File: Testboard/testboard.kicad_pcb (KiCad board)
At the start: 2 copper layers, 0 parts

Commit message: :sparkles: PCB layout for the testboard
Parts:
- added C1: 100n, Capacitor_THT:C_Disc_D4.3mm_W1.9mm_P5.00mm, F.Cu at (83.8, 111.7)
- added C2: 10n, Capacitor_THT:C_Disc_D4.3mm_W1.9mm_P5.00mm, F.Cu at (83.9, 102.9)
- added C3: 100n, Capacitor_THT:C_Disc_D4.3mm_W1.9mm_P5.00mm, F.Cu at (95.9, 106.7)
- added C4: 10n, Capacitor_THT:C_Disc_D4.3mm_W1.9mm_P5.00mm, F.Cu at (111.1, 99.0)
- added C5: 100n, Capacitor_THT:C_Disc_D4.3mm_W1.9mm_P5.00mm, F.Cu at (114.3, 101.7)
- added C6: 100n, Capacitor_THT:C_Disc_D4.3mm_W1.9mm_P5.00mm, F.Cu at (111.1, 101.6)
- added C7: 100n, Capacitor_THT:C_Disc_D4.3mm_W1.9mm_P5.00mm, F.Cu at (106.6, 95.2)
- added D1: rt, LED_THT:LED_D3.0mm, F.Cu at (107.3, 78.1)
- added J1: upper, Connector_PinSocket_2.54mm:PinSocket_2x02_P2.54mm_Vertical, F.Cu at (81.3, 79.5)
- added J2: lower, Connector_PinSocket_2.54mm:PinSocket_2x02_P2.54mm_Vertical, F.Cu at (81.3, 124.5)
- added J3: Out, Connector_PinHeader_2.54mm:PinHeader_1x02_P2.54mm_Vertical, F.Cu at (116.2, 78.7)
- added J4: Out, Connector_PinHeader_2.54mm:PinHeader_1x02_P2.54mm_Vertical, F.Cu at (112.4, 78.7)
- added J5: V_{drive}, Connector_PinHeader_2.54mm:PinHeader_1x02_P2.54mm_Vertical, F.Cu at (90.8, 118.7)
- added Q1: BC547, Package_TO_SOT_THT:TO-92_Inline, F.Cu at (98.4, 86.3)
- added R1: 100R, Resistor_THT:R_Axial_DIN0207_L6.3mm_D2.5mm_P7.62mm_Horizontal, F.Cu at (80.0, 114.2)
- added R10: 1k, Resistor_THT:R_Axial_DIN0207_L6.3mm_D2.5mm_P7.62mm_Horizontal, F.Cu at (103.5, 85.1)
- added R2: 2k2, Resistor_THT:R_Axial_DIN0207_L6.3mm_D2.5mm_P7.62mm_Horizontal, F.Cu at (80.0, 102.9)
- added R3: 10k, Resistor_THT:R_Axial_DIN0207_L6.3mm_D2.5mm_P7.62mm_Horizontal, F.Cu at (92.7, 102.9)
- added R4: 10k, Resistor_THT:R_Axial_DIN0207_L6.3mm_D2.5mm_P7.62mm_Horizontal, F.Cu at (92.7, 106.7)
- added R5: 4k7, Resistor_THT:R_Axial_DIN0207_L6.3mm_D2.5mm_P7.62mm_Horizontal, F.Cu at (114.3, 99.0)
- added R6: 470R, Resistor_THT:R_Axial_DIN0207_L6.3mm_D2.5mm_P7.62mm_Horizontal, F.Cu at (103.5, 91.4)
- added R7: 2k2, Resistor_THT:R_Axial_DIN0207_L6.3mm_D2.5mm_P7.62mm_Horizontal, F.Cu at (96.5, 102.9)
- added R8: 10k, Resistor_THT:R_Axial_DIN0207_L6.3mm_D2.5mm_P7.62mm_Horizontal, F.Cu at (92.7, 90.2)
- added R9: 1k, Resistor_THT:R_Axial_DIN0207_L6.3mm_D2.5mm_P7.62mm_Horizontal, F.Cu at (103.5, 88.3)
- added RV1: 1M, Potentiometer_THT:Potentiometer_Piher_PT-10-V10_Vertical, F.Cu at (85.2, 85.2)
- added SW1: SW_Push, Button_Switch_Keyboard:SW_Cherry_MX_1.00u_PCB, F.Cu at (111.1, 114.3)
- added SW2: ON/ON, moPsy:PB_Hor_7x7_2pole_2.5mm, F.Cu at (86.4, 93.3)
- added TP1: IN, TestPoint:TestPoint_Loop_D1.80mm_Drill1.0mm_Beaded, F.Cu at (86.4, 126.4)
- added TP2: TRIGGER_IN, TestPoint:TestPoint_Loop_D1.80mm_Drill1.0mm_Beaded, F.Cu at (91.4, 126.4)
- added TP3: TR, TestPoint:TestPoint_Loop_D1.80mm_Drill1.0mm_Beaded, F.Cu at (96.5, 126.4)
- added TP4: TRIGGER_OUT, TestPoint:TestPoint_Loop_D1.80mm_Drill1.0mm_Beaded, F.Cu at (101.0, 80.0)
- added TP5: OUT, TestPoint:TestPoint_Loop_D1.80mm_Drill1.0mm_Beaded, F.Cu at (115.6, 87.0)
- added U1: LM555xN, Package_DIP:DIP-8_W7.62mm, F.Cu at (100.3, 99.1)
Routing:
- net +12V: track 0.00 -> 78.8 mm
- net Net-(SW2-B): track 0.00 -> 45.4 mm
- net /TRIGGER_OUT: track 0.00 -> 43.4 mm
- net /TRIGGER_IN: track 0.00 -> 42.4 mm
- net Net-(R1-Pad1): track 0.00 -> 40.6 mm
- net Net-(J5-Pin_2): track 0.00 -> 38.6 mm
- net Net-(R5-Pad2): track 0.00 -> 25.5 mm
- net Net-(J3-Pin_1): track 0.00 -> 14.5 mm
- net Net-(D1-A): track 0.00 -> 12.4 mm
- net Net-(U1-DIS): track 0.00 -> 11.5 mm
- net Net-(U1-CV): track 0.00 -> 11.3 mm
- net Net-(Q1-B): track 0.00 -> 10.2 mm
- net Net-(Q1-E): track 0.00 -> 9.79 mm
- net Net-(U1-R): track 0.00 -> 7.66 mm
- net Net-(J4-Pin_1): track 0.00 -> 6.88 mm
- added copper zone on B.Cu, net GND
- added copper zone on F.Cu, net GND
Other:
- board outline added: 42.5 x 54 mm
- board text added: "CC BY-SA 4.0 Stefan Haun"
- board text added: "Connect to Eurorack Power Breakout"
- board text added: "IN"
- board text added: "OUT"
- board text added: "TR"
- board text added: "TR IN"
- board text added: "TRG OUT"
- board text added: "Testboard v1"
- board text added: "V_{drive}"
- board text added: "https://github.com/moPsy-project/manual-gate-trigger-source"

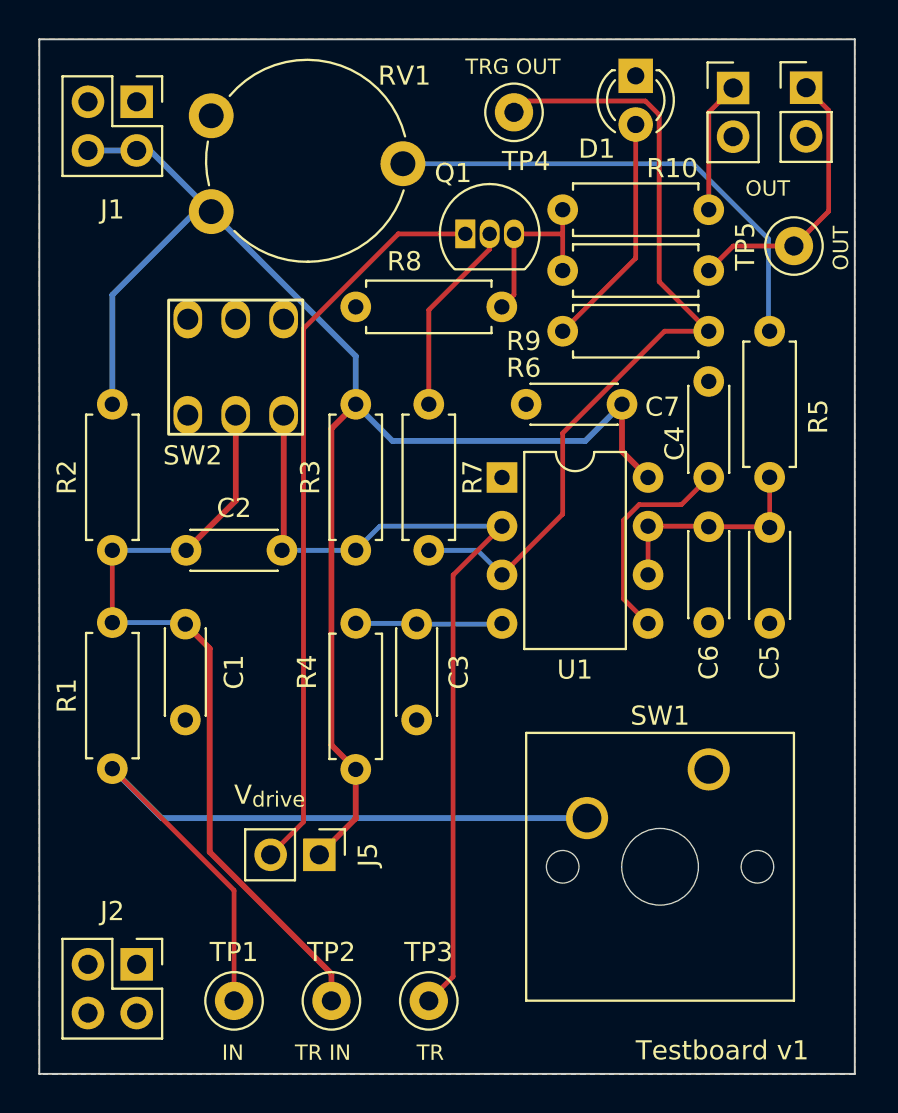
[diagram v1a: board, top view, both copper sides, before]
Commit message: :hammer: Adapt PCB to schematic changes
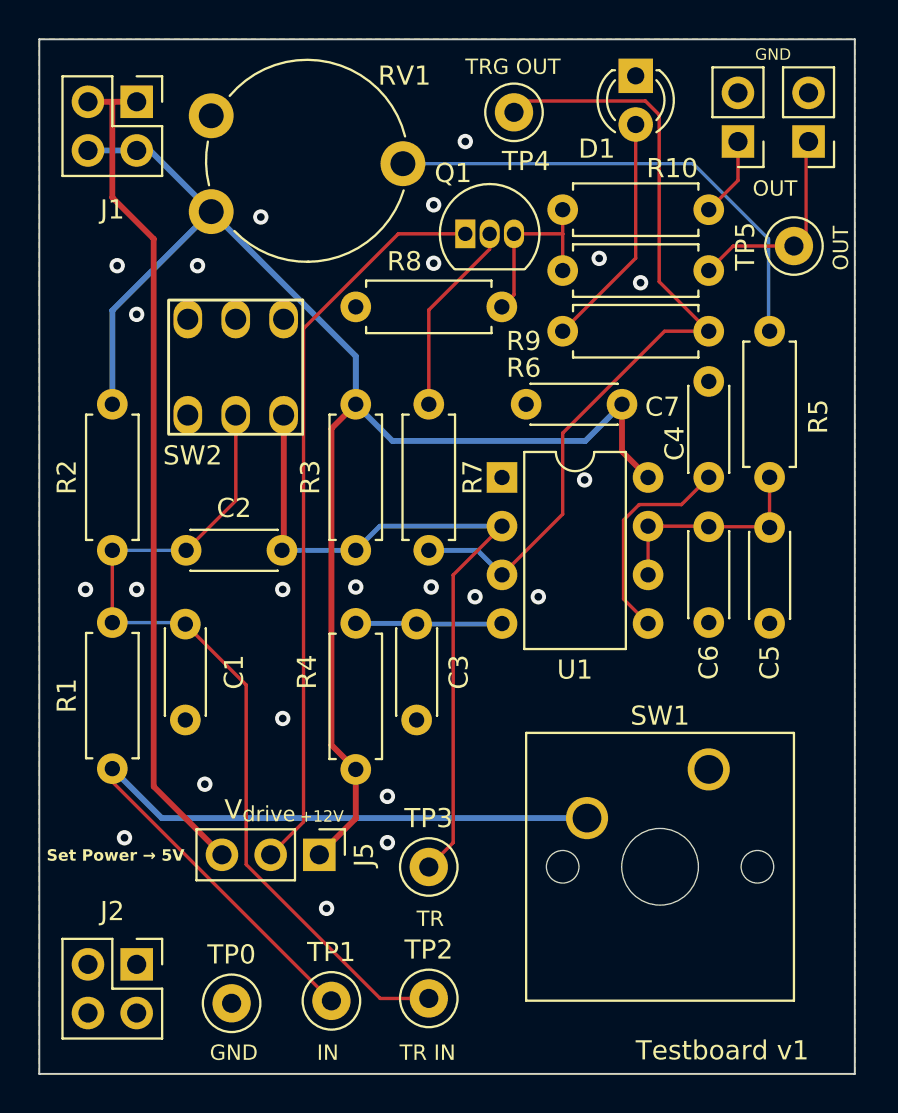
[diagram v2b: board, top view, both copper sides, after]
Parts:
- added TP0: GND, TestPoint:TestPoint_Loop_D1.80mm_Drill1.0mm_Beaded, F.Cu at (86.2, 126.5)
- J5: footprint Connector_PinHeader_2.54mm:PinHeader_1x02_P2.54mm_Vertical -> Connector_PinHeader_2.54mm:PinHeader_1x03_P2.54mm_Vertical
- moved TP3 6.98 mm to (96.5, 119.4)
- moved TP2 5.08 mm to (96.5, 126.2)
- moved TP1 5.08 mm to (91.4, 126.4)
- moved J3 2.81 mm to (116.3, 81.5), turned to 180 degrees
- moved J4 2.81 mm to (112.6, 81.5), turned to 180 degrees
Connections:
- J1 pad 1: unconnected-(J1-Pin_1-Pad1) -> Vdrive
- J1 pad 2: unconnected-(J1-Pin_2-Pad2) -> Vdrive
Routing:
- net Vdrive: track 0.00 -> 44.2 mm
- net Net-(SW2-B): track 45.4 -> 38.4 mm
- net Net-(J3-Pin_1): track 14.5 -> 10.7 mm
- net /TRIGGER_IN: track 42.4 -> 45.8 mm
- net Net-(J4-Pin_1): track 6.88 -> 4.19 mm
- net Net-(R1-Pad1): track 40.6 -> 42.7 mm
- net GND: vias 0 -> 23
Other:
- board text added: "+12V"
- board text added: "GND"
- board text added: "Set Power → 5V"
